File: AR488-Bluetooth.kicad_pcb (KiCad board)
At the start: 2 copper layers, 93.5 x 57.9 mm, 18 parts, among them J1 112-024-213R001, J3 HC-05, P2 Power, P3 Analog, P4 Analog, P5 PWM, P6 PWM, P7 Communication, U1 SN75160BN, U2 SN75161BN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

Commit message: PCB Tune Length
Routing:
- net /16(Tx2): track 11.8 -> 53.7 mm, vias 0 -> 2
- net /17(Rx2): track 15.9 -> 55.2 mm
- net /GPIB10: track 14.5 -> 41.6 mm
- net /9(**): track 56.6 -> 81.9 mm
- net /GPIB11: track 17.9 -> 41.7 mm
- net /6(**): track 34.8 -> 55.3 mm
- net /7(**): track 39.5 -> 55.3 mm
- net /GPIB6: track 27.1 -> 40.3 mm
- net /GPIB7: track 27.5 -> 40.3 mm
- net /GPIB9: track 29.6 -> 41.8 mm
- net /GPIB5: track 28.5 -> 40.3 mm
- net /GPIB8: track 28.8 -> 40.3 mm
- net /GPIB4: track 29.3 -> 40.2 mm
- net /GPIB16: track 51.2 -> 40.3 mm, vias 3 -> 1
- net /GPIB15: track 50.1 -> 40.3 mm, vias 3 -> 1
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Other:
- board text added: "AR488 GPIB Hat Arduino Mega 2560 2022/01/18"
- board text removed: "AR488 GPIB Hat Arduino Mega 2560 2021/12/20"

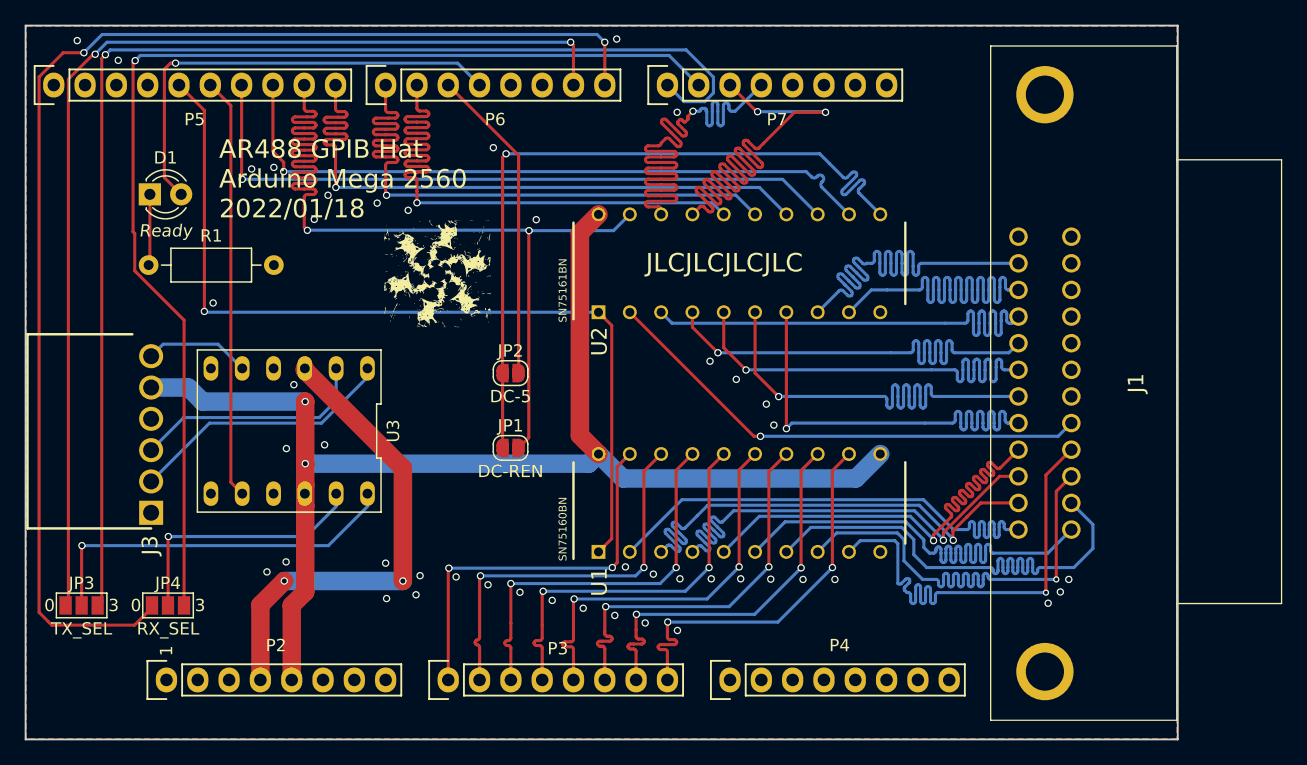
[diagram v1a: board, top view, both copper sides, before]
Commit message: Correct the design and add the battery circuit. No Gerber is generated
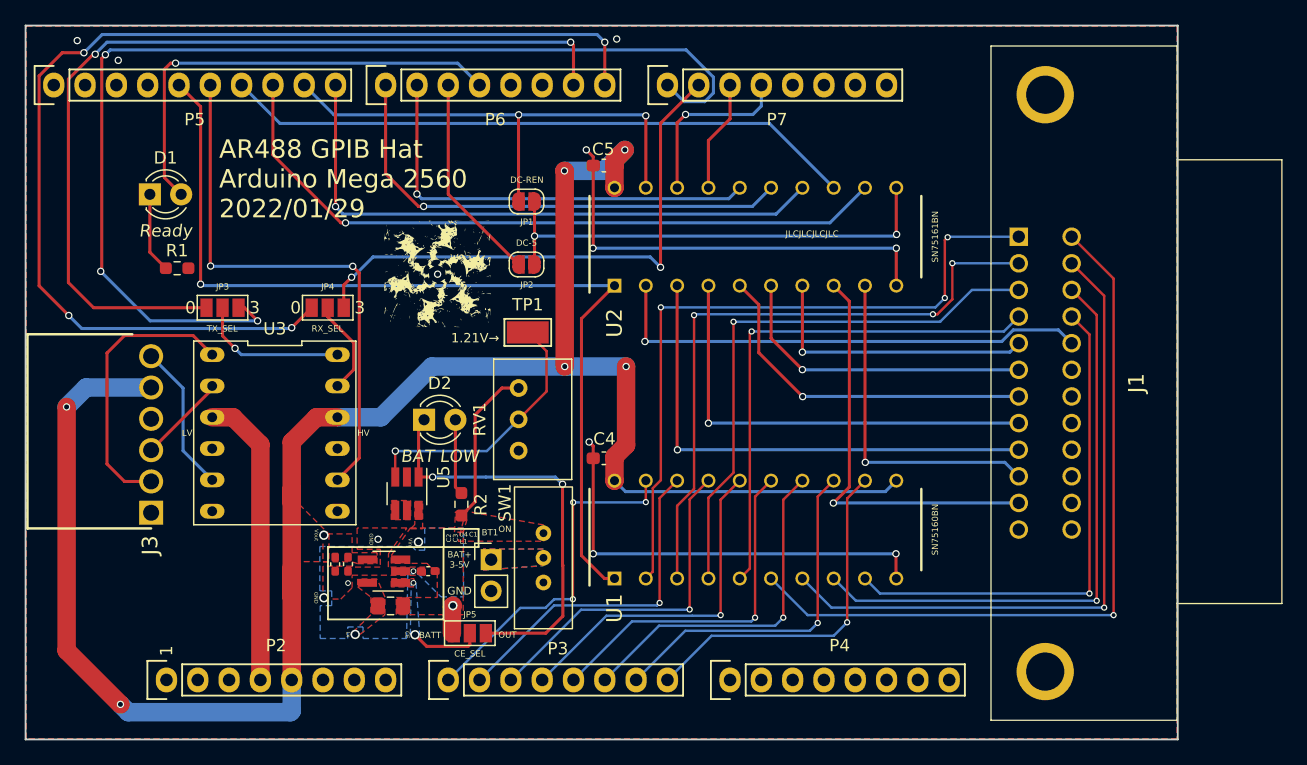
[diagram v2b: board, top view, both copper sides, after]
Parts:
- added BT1: Battery, Connector_PinHeader_2.54mm:PinHeader_1x02_P2.54mm_Vertical, F.Cu at (157.7, 109.4)
- added C1: 10u, Capacitor_SMD:C_0402_1005Metric_Pad0.74x0.62mm_HandSolder, F.Cu at (152.5, 110.3)
- added C2: 10u, Capacitor_SMD:C_0402_1005Metric_Pad0.74x0.62mm_HandSolder, F.Cu at (145.0, 109.7)
- added C3: 10u, Capacitor_SMD:C_0402_1005Metric_Pad0.74x0.62mm_HandSolder, F.Cu at (146.0, 109.7)
- added C4: 0.1u, Capacitor_SMD:C_0603_1608Metric_Pad1.08x0.95mm_HandSolder, F.Cu at (166.8, 101.1)
- added C5: 0.1u, Capacitor_SMD:C_0603_1608Metric_Pad1.08x0.95mm_HandSolder, F.Cu at (166.8, 77.4)
- added D2: BAT LOW, LED_THT:LED_D3.0mm, F.Cu at (152.2, 98.0)
- added JP5: CE_SEL, Jumper:SolderJumper-3_P1.3mm_Open_Pad1.0x1.5mm_NumberLabels, F.Cu at (155.9, 115.3)
- added L1: 4.7u, Inductor_SMD:L_0805_2012Metric_Pad1.15x1.40mm_HandSolder, F.Cu at (149.5, 113.1)
- added R2: 1k, Resistor_SMD:R_0603_1608Metric_Pad0.98x0.95mm_HandSolder, F.Cu at (155.2, 104.9)
- added RV1: 5M, Potentiometer_THT:Potentiometer_Bourns_3299W_Vertical, F.Cu at (159.9, 95.4)
- added SW1: SW_SPDT, Socket_Arduino_Mega:STSSS9121, F.Cu at (161.9, 111.2)
- added TP1: TestPoint, TestPoint:TestPoint_Keystone_5015_Micro-Minature, F.Cu at (160.6, 90.9)
- added U4: XC9141B50CMR-G, Package_TO_SOT_SMD:SOT-23-5_HandSoldering, F.Cu at (149.0, 110.3)
- added U5: MCP65R41T-1202E/CHY, Package_TO_SOT_SMD:SOT-23-6_Handsoldering, F.Cu at (150.8, 104.0)
- R1: footprint Resistor_THT:R_Axial_DIN0207_L6.3mm_D2.5mm_P10.16mm_Horizontal -> Resistor_SMD:R_0603_1608Metric_Pad0.98x0.95mm_HandSolder
- moved JP4 27.4 mm to (144.4, 88.9)
- moved JP3 26.7 mm to (135.9, 88.9)
- moved JP1 20.0 mm to (160.5, 80.3), turned to 180 degrees
- moved JP2 8.91 mm to (160.5, 85.4), turned to 180 degrees
- moved U2 2.52 mm to (179.1, 83.2)
- moved U1 2.52 mm to (179.1, 106.9)
- moved R1 2.33 mm to (132.2, 85.7)
- moved U3 2.17 mm to (141.1, 98.1), turned to 0 degrees
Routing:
- net GND: track 0.00 -> 71.7 mm, vias 45 -> 14
- net +5V: track 105.3 -> 160.8 mm, vias 2 -> 7
- net /15(Rx3): track 92.9 -> 44.9 mm, vias 1 -> 2
- net /16(Tx2): track 53.7 -> 9.06 mm, vias 2 -> 0
- net /17(Rx2): track 55.2 -> 14.4 mm
- net /9(**): track 81.9 -> 41.6 mm
- net /CE_OUT: track 0.00 -> 34.3 mm, vias 0 -> 2
- net Net-(JP1-Pad1): track 61.5 -> 38.3 mm, vias 1 -> 2
- net /IN+: track 0.00 -> 21.8 mm, vias 0 -> 1
- net /6(**): track 55.3 -> 35.6 mm
- net /GPIB13: track 41.8 -> 61.1 mm, vias 0 -> 1
- net Net-(JP3-Pad2): track 29.4 -> 12.2 mm
- net /GPIB5: track 40.3 -> 23.3 mm
- net +BATT: track 0.00 -> 15.3 mm, vias 0 -> 2
- net /7(**): track 55.3 -> 40.2 mm
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- added copper zone on F.Cu, net +5V
- added copper zone on F.Cu, net +BATT
- added copper zone on B.Cu, net /BAT_IN
- added copper zone on F.Cu, net /BAT_IN
- added copper zone on B.Cu, net /CE
- added copper zone on F.Cu, net /CE
- added copper zone on F.Cu, net /IN-
- added copper zone on F.Cu, net /Lx
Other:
- board text added: "1.21V→"
- board text added: "AR488 GPIB Hat Arduino Mega 2560 2022/01/29"
- board text added: "BAT+ 3-5V"
- board text added: "CE"
- board text added: "GND"
- board text added: "HV"
- board text added: "LV"
- board text added: "Lx"
- board text added: "ON"
- board text added: "Vin"
- board text added: "Vout"
- board text removed: "AR488 GPIB Hat Arduino Mega 2560 2022/01/18"

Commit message: Update the images and connect shield to GND
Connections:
- J1 pad MH1: unconnected-(J1-PadMH1) -> GND
- J1 pad MH2: unconnected-(J1-PadMH2) -> GND
